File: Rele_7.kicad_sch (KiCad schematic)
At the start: 5 parts

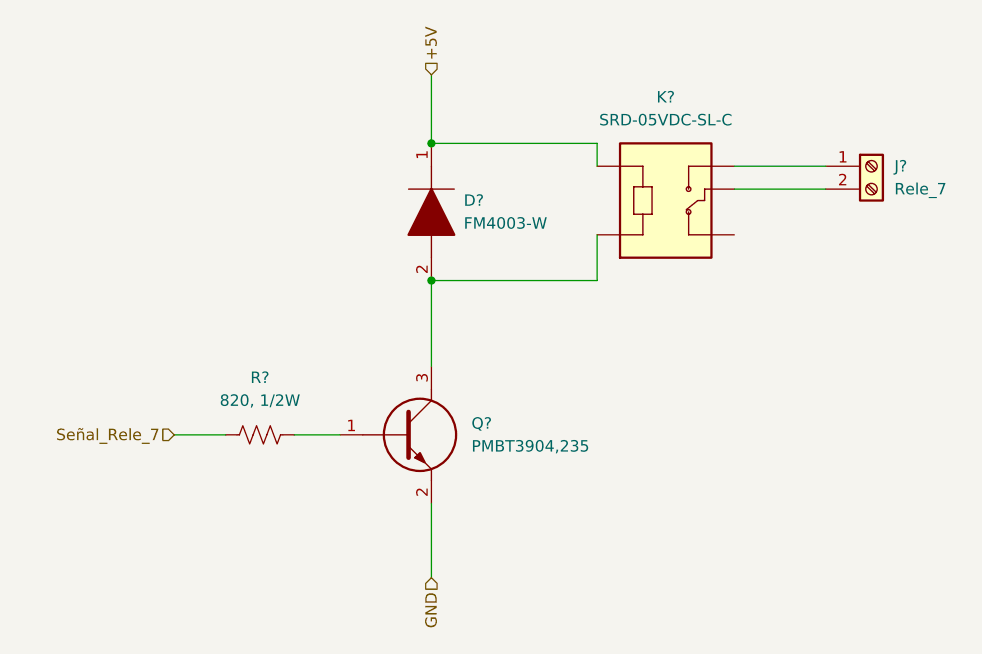
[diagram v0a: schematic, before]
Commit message: Ajuste del esquematico
Se cambio el integrado ESP32 por 2 tiras de pines de 1x15, se quitaron los switches EN y BOOT que ya estan en el NodeMCU, se quito el mutliplexor 74HC y se cablearon las I/O
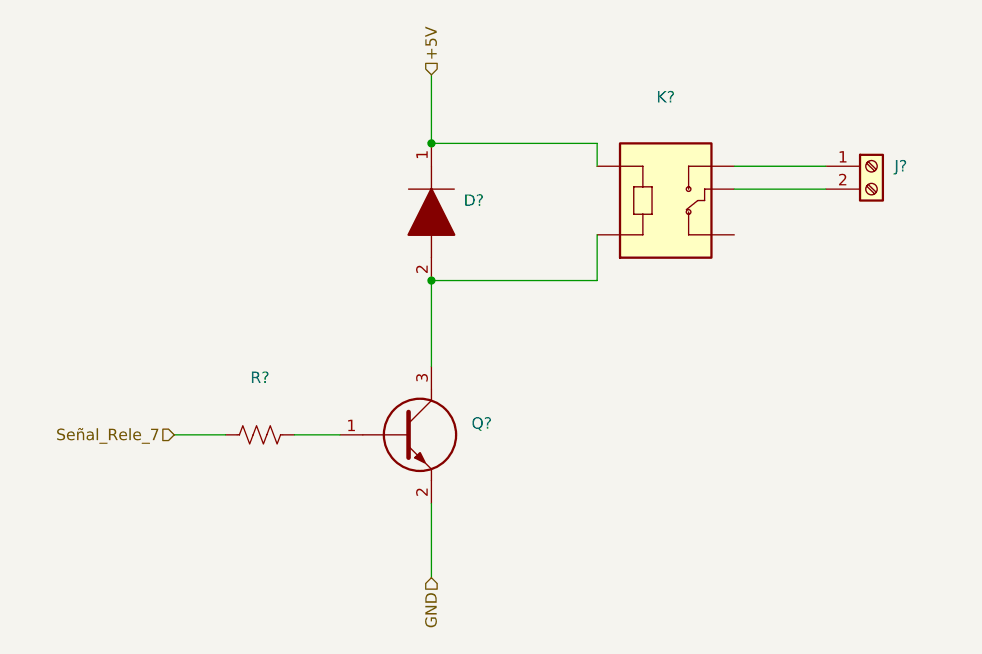
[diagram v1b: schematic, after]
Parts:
- D?: value FM4003-W -> (none); footprint DIOM5025X231N -> (none)
- J?: value Rele_7 -> (none)
- K?: value SRD-05VDC-SL-C -> (none); footprint RELAY_SRD-05VDC-SL-C -> (none)
- Q?: value PMBT3904,235 -> (none); footprint SOT95P230X110-3N -> (none)
- R?: value 820, 1/2W -> (none)
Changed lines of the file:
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@@
     (in_bom yes) (on_board yes) (fields_autoplaced)
     (property "Reference" "R?" (id 0) (at 125.095 101.6 90))
-    (property "Value" "820, 1/2W" (id 1) (at 125.095 104.14 90))
+    (property "Value" "" (id 1) (at 125.095 104.14 90))
     (property "Footprint" "" (id 2) (at 125.349 106.934 90)
       (effects (font (size 1.27 1.27)) hide)
@@
       (effects (font (size 1.27 1.27)) (justify left))
     )
-    (property "Value" "FM4003-W" (id 1) (at 147.7264 84.4549 90)
+    (property "Value" "" (id 1) (at 147.7264 84.4549 90)
       (effects (font (size 1.27 1.27)) (justify left))
     )
-    (property "Footprint" "DIOM5025X231N" (id 2) (at 144.145 86.995 0)
+    (property "Footprint" "" (id 2) (at 144.145 86.995 0)
       (effects (font (size 1.27 1.27)) (justify left) hide)
     )
@@
       (effects (font (size 1.27 1.27)) (justify left))
     )
-    (property "Value" "Rele_7" (id 1) (at 195.58 80.6449 0)
+    (property "Value" "" (id 1) (at 195.58 80.6449 0)
       (effects (font (size 1.27 1.27)) (justify left))
     )
@@
     (in_bom yes) (on_board yes) (fields_autoplaced)
     (property "Reference" "K?" (id 0) (at 170.18 70.4342 0))
-    (property "Value" "SRD-05VDC-SL-C" (id 1) (at 170.18 72.9742 0))
-    (property "Footprint" "RELAY_SRD-05VDC-SL-C" (id 2) (at 170.18 80.645 0)
+    (property "Value" "" (id 1) (at 170.18 72.9742 0))
+    (property "Footprint" "" (id 2) (at 170.18 80.645 0)
       (effects (font (size 1.27 1.27)) (justify left bottom) hide)
     )
@@
       (effects (font (size 1.27 1.27)) (justify left))
     )
-    (property "Value" "PMBT3904,235" (id 1) (at 148.59 109.2199 0)
+    (property "Value" "" (id 1) (at 148.59 109.2199 0)
       (effects (font (size 1.27 1.27)) (justify left))
     )
-    (property "Footprint" "SOT95P230X110-3N" (id 2) (at 147.955 111.76 0)
+    (property "Footprint" "" (id 2) (at 147.955 111.76 0)
       (effects (font (size 1.27 1.27)) (justify left) hide)
     )

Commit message: Modificación de posición de circ. filtrado y circ. de adaptación de tensión
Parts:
- D?, J?, K?, Q?, R?: value (none) -> ~
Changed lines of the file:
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@@
     (in_bom yes) (on_board yes) (fields_autoplaced)
     (property "Reference" "R?" (id 0) (at 125.095 101.6 90))
-    (property "Value" "" (id 1) (at 125.095 104.14 90))
+    (property "Value" "~" (id 1) (at 125.095 104.14 90))
     (property "Footprint" "" (id 2) (at 125.349 106.934 90)
       (effects (font (size 1.27 1.27)) hide)
@@
       (effects (font (size 1.27 1.27)) (justify left))
     )
-    (property "Value" "" (id 1) (at 147.7264 84.4549 90)
+    (property "Value" "~" (id 1) (at 147.7264 84.4549 90)
       (effects (font (size 1.27 1.27)) (justify left))
     )
@@
       (effects (font (size 1.27 1.27)) (justify left))
     )
-    (property "Value" "" (id 1) (at 195.58 80.6449 0)
+    (property "Value" "~" (id 1) (at 195.58 80.6449 0)
       (effects (font (size 1.27 1.27)) (justify left))
     )
@@
     (in_bom yes) (on_board yes) (fields_autoplaced)
     (property "Reference" "K?" (id 0) (at 170.18 70.4342 0))
-    (property "Value" "" (id 1) (at 170.18 72.9742 0))
+    (property "Value" "~" (id 1) (at 170.18 72.9742 0))
     (property "Footprint" "" (id 2) (at 170.18 80.645 0)
       (effects (font (size 1.27 1.27)) (justify left bottom) hide)
@@
       (effects (font (size 1.27 1.27)) (justify left))
     )
-    (property "Value" "" (id 1) (at 148.59 109.2199 0)
+    (property "Value" "~" (id 1) (at 148.59 109.2199 0)
       (effects (font (size 1.27 1.27)) (justify left))
     )

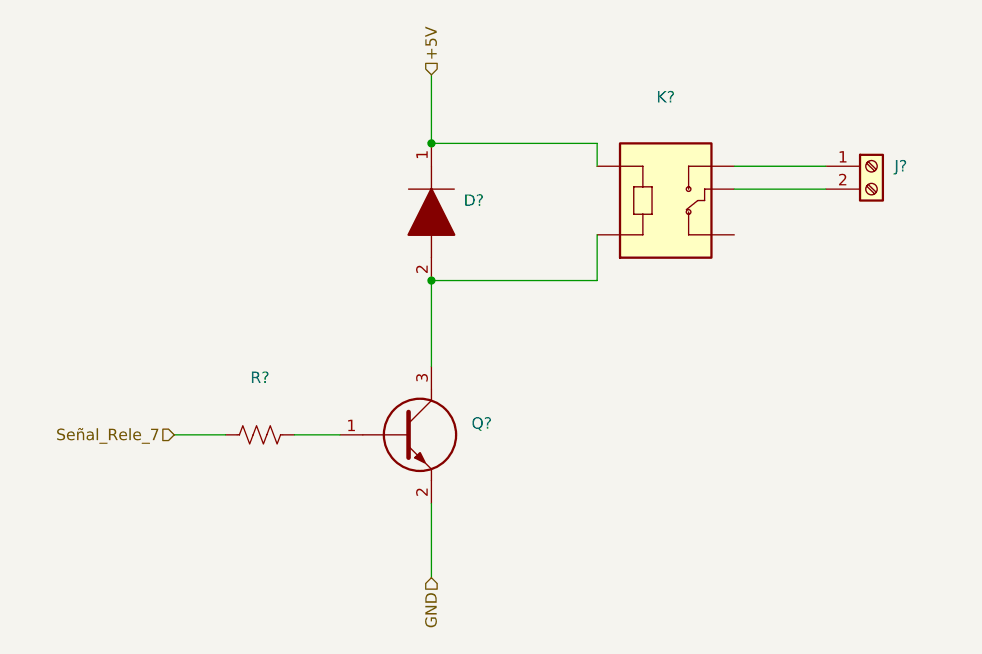
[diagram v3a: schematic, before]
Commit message: Actualización de SCH según placa industrial, y búsqueda de footprints.
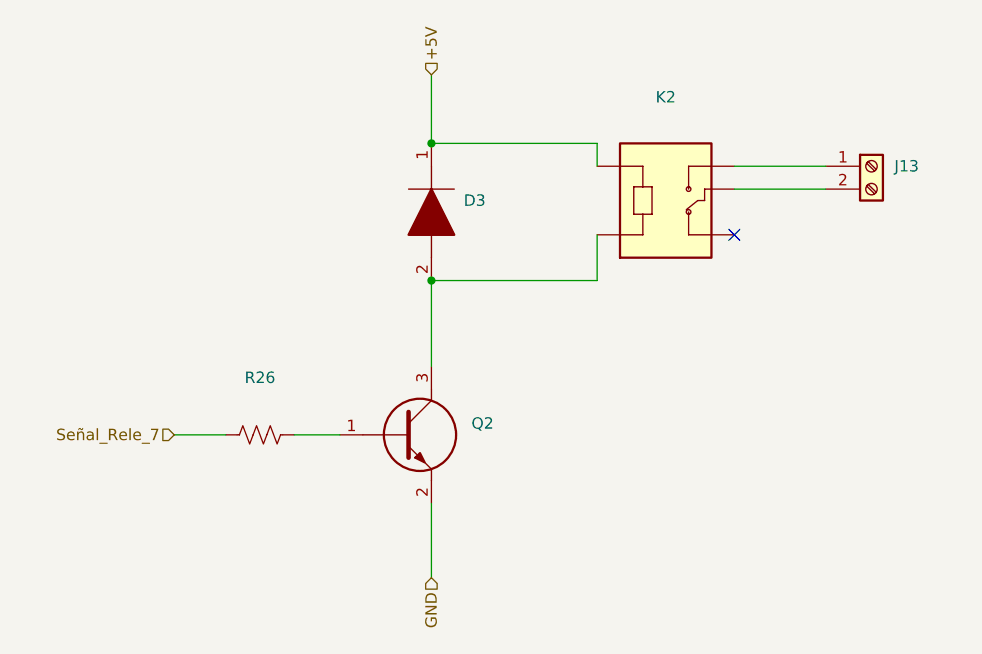
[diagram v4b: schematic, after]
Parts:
- D3: renamed from D?; value ~ -> (none)
- J13: renamed from J?; value ~ -> (none)
- K2: renamed from K?; value ~ -> (none)
- Q2: renamed from Q?; value ~ -> (none)
- R26: renamed from R?; value ~ -> (none)
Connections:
- no-connect marks 0 -> 1
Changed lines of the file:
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@@
   (junction (at 144.145 90.805) (diameter 0) (color 0 0 0 0)
   )
+  (no_connect (at 177.8 85.725))
   (wire (pts (xy 144.145 90.805) (xy 162.56 90.805))
     (stroke (width 0) (type default) (color 0 0 0 0))
@@
   (symbol (lib_id "Device:R_US") (at 125.095 107.95 90) (unit 1)
     (in_bom yes) (on_board yes) (fields_autoplaced)
-    (property "Reference" "R?" (id 0) (at 125.095 101.6 90))
-    (property "Value" "~" (id 1) (at 125.095 104.14 90))
+    (property "Reference" "R26" (id 0) (at 125.095 101.6 90))
+    (property "Value" "" (id 1) (at 125.095 104.14 90))
     (property "Footprint" "" (id 2) (at 125.349 106.934 90)
       (effects (font (size 1.27 1.27)) hide)
@@
   (symbol (lib_id "FM4003-W:FM4003-W") (at 144.145 75.565 270) (unit 1)
     (in_bom yes) (on_board yes) (fields_autoplaced)
-    (property "Reference" "D?" (id 0) (at 147.7264 81.9149 90)
+    (property "Reference" "D3" (id 0) (at 147.7264 81.9149 90)
       (effects (font (size 1.27 1.27)) (justify left))
     )
-    (property "Value" "~" (id 1) (at 147.7264 84.4549 90)
+    (property "Value" "" (id 1) (at 147.7264 84.4549 90)
       (effects (font (size 1.27 1.27)) (justify left))
     )
@@
   (symbol (lib_id "Connector:Screw_Terminal_01x02") (at 193.04 78.105 0) (unit 1)
     (in_bom yes) (on_board yes) (fields_autoplaced)
-    (property "Reference" "J?" (id 0) (at 195.58 78.1049 0)
+    (property "Reference" "J13" (id 0) (at 195.58 78.1049 0)
       (effects (font (size 1.27 1.27)) (justify left))
     )
-    (property "Value" "~" (id 1) (at 195.58 80.6449 0)
+    (property "Value" "" (id 1) (at 195.58 80.6449 0)
       (effects (font (size 1.27 1.27)) (justify left))
     )
@@
   (symbol (lib_id "SRD-05VDC-SL-C:SRD-05VDC-SL-C") (at 170.18 80.645 0) (unit 1)
     (in_bom yes) (on_board yes) (fields_autoplaced)
-    (property "Reference" "K?" (id 0) (at 170.18 70.4342 0))
-    (property "Value" "~" (id 1) (at 170.18 72.9742 0))
+    (property "Reference" "K2" (id 0) (at 170.18 70.4342 0))
+    (property "Value" "" (id 1) (at 170.18 72.9742 0))
     (property "Footprint" "" (id 2) (at 170.18 80.645 0)
       (effects (font (size 1.27 1.27)) (justify left bottom) hide)
@@
   (symbol (lib_id "PMBT3904,235:PMBT3904,235") (at 133.985 107.95 0) (unit 1)
     (in_bom yes) (on_board yes) (fields_autoplaced)
-    (property "Reference" "Q?" (id 0) (at 148.59 106.6799 0)
+    (property "Reference" "Q2" (id 0) (at 148.59 106.6799 0)
       (effects (font (size 1.27 1.27)) (justify left))
     )
-    (property "Value" "~" (id 1) (at 148.59 109.2199 0)
+    (property "Value" "" (id 1) (at 148.59 109.2199 0)
       (effects (font (size 1.27 1.27)) (justify left))
     )

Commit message: Fin de SCH, config de inicio para PCB
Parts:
- D3: value (none) -> FM4003-W; footprint (none) -> FM4003W:DIOM5025X231N
- J13: value (none) -> Rele_7; footprint (none) -> TB002-500-02BE:TB00250002BE
- K2: value (none) -> SRD-05VDC-SL-C; footprint (none) -> SRD-05VDC-SL-C-Version_2:RELAY_SRD-05VDC-SL-C
- Q2: value (none) -> PMBT3904,235; footprint (none) -> PMBT3904,235:SOT95P230X110-3N
- R26: value (none) -> 820, 1/2W; footprint (none) -> Resistor_SMD:R_0805_2012Metric
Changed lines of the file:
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@@
     (in_bom yes) (on_board yes) (fields_autoplaced)
     (property "Reference" "R26" (id 0) (at 125.095 101.6 90))
-    (property "Value" "" (id 1) (at 125.095 104.14 90))
-    (property "Footprint" "" (id 2) (at 125.349 106.934 90)
+    (property "Value" "820, 1/2W" (id 1) (at 125.095 104.14 90))
+    (property "Footprint" "Resistor_SMD:R_0805_2012Metric" (id 2) (at 125.349 106.934 90)
       (effects (font (size 1.27 1.27)) hide)
     )
@@
       (effects (font (size 1.27 1.27)) (justify left))
     )
-    (property "Value" "" (id 1) (at 147.7264 84.4549 90)
+    (property "Value" "FM4003-W" (id 1) (at 147.7264 84.4549 90)
       (effects (font (size 1.27 1.27)) (justify left))
     )
-    (property "Footprint" "" (id 2) (at 144.145 86.995 0)
+    (property "Footprint" "FM4003W:DIOM5025X231N" (id 2) (at 144.145 86.995 0)
       (effects (font (size 1.27 1.27)) (justify left) hide)
     )
@@
       (effects (font (size 1.27 1.27)) (justify left))
     )
-    (property "Value" "" (id 1) (at 195.58 80.6449 0)
+    (property "Value" "Rele_7" (id 1) (at 195.58 80.6449 0)
       (effects (font (size 1.27 1.27)) (justify left))
     )
-    (property "Footprint" "" (id 2) (at 193.04 78.105 0)
+    (property "Footprint" "TB002-500-02BE:TB00250002BE" (id 2) (at 193.04 78.105 0)
       (effects (font (size 1.27 1.27)) hide)
     )
@@
     (in_bom yes) (on_board yes) (fields_autoplaced)
     (property "Reference" "K2" (id 0) (at 170.18 70.4342 0))
-    (property "Value" "" (id 1) (at 170.18 72.9742 0))
-    (property "Footprint" "" (id 2) (at 170.18 80.645 0)
+    (property "Value" "SRD-05VDC-SL-C" (id 1) (at 170.18 72.9742 0))
+    (property "Footprint" "SRD-05VDC-SL-C-Version_2:RELAY_SRD-05VDC-SL-C" (id 2) (at 170.18 80.645 0)
       (effects (font (size 1.27 1.27)) (justify left bottom) hide)
     )
@@
       (effects (font (size 1.27 1.27)) (justify left))
     )
-    (property "Value" "" (id 1) (at 148.59 109.2199 0)
+    (property "Value" "PMBT3904,235" (id 1) (at 148.59 109.2199 0)
       (effects (font (size 1.27 1.27)) (justify left))
     )
-    (property "Footprint" "" (id 2) (at 147.955 111.76 0)
+    (property "Footprint" "PMBT3904,235:SOT95P230X110-3N" (id 2) (at 147.955 111.76 0)
       (effects (font (size 1.27 1.27)) (justify left) hide)
     )

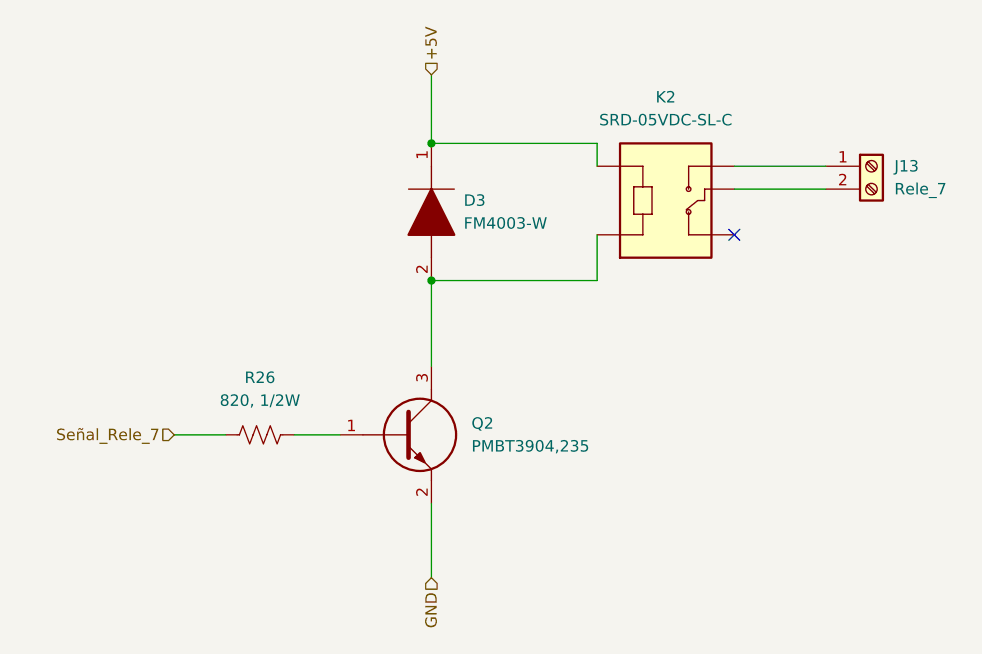
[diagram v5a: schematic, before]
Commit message: Cambios en SCH y PCB.
Se cambio el adaptador de nivel 5-3,3V por un circuito con MOSFET 2N7002, dado que ya no hay stock del NXB. Se modificó el footprint del expansor I/O por uno thorugh-hole.
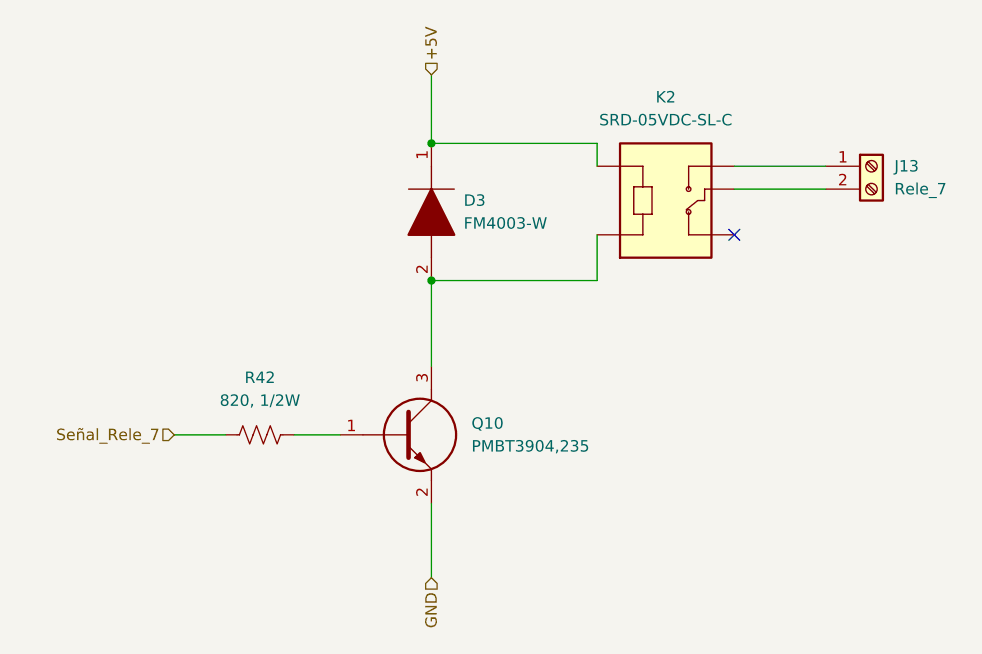
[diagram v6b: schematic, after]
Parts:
- renumbered Q2 to Q10, R26 to R42
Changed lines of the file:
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@@
   (symbol (lib_id "Device:R_US") (at 125.095 107.95 90) (unit 1)
     (in_bom yes) (on_board yes) (fields_autoplaced)
-    (property "Reference" "R26" (id 0) (at 125.095 101.6 90))
+    (property "Reference" "R42" (id 0) (at 125.095 101.6 90))
     (property "Value" "820, 1/2W" (id 1) (at 125.095 104.14 90))
     (property "Footprint" "Resistor_SMD:R_0805_2012Metric" (id 2) (at 125.349 106.934 90)
@@
   (symbol (lib_id "PMBT3904,235:PMBT3904,235") (at 133.985 107.95 0) (unit 1)
     (in_bom yes) (on_board yes) (fields_autoplaced)
-    (property "Reference" "Q2" (id 0) (at 148.59 106.6799 0)
+    (property "Reference" "Q10" (id 0) (at 148.59 106.6799 0)
       (effects (font (size 1.27 1.27)) (justify left))
     )
